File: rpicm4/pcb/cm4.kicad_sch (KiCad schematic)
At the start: 3 parts

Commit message: rpicm4
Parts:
- removed Module?: ComputeModule4-CM4, CM4IO:Raspberry-Pi-4-Compute-Module, symbol CM4IO:ComputeModule4-CM4
- added Module1: ComputeModule4-CM4, CM4IO:Raspberry-Pi-4-Compute-Module, symbol CM4IO:ComputeModule4-CM4
- J1, J2: renamed from J?; footprint (none) -> Connector_USB:USB_C_Receptacle_XKB_U262-16XN-4BVC11
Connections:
- net GND: now reaches J2.A1 (GND), J2.A12 (GND), J2.B1 (GND), J2.B12 (GND)
- net GND: now also J1.A1 (GND), J1.A12 (GND), J1.B1 (GND), J1.B12 (GND), J1.S1 (SHIELD), J2.S1 (SHIELD), Module1.1 (GND), Module1.107 (GND), Module1.108 (GND), Module1.113 (GND), Module1.114 (GND), Module1.119 (GND), Module1.120 (GND), Module1.125 (GND), Module1.126 (GND), Module1.13 (GND), Module1.131 (GND), Module1.132 (GND), Module1.137 (GND), Module1.138 (GND), Module1.14 (GND), Module1.144 (GND), Module1.150 (GND), Module1.155 (GND), Module1.156 (GND), Module1.161 (GND), Module1.162 (GND), Module1.167 (GND), Module1.168 (GND), Module1.173 (GND), Module1.179 (GND), Module1.180 (GND), Module1.185 (GND), Module1.186 (GND), Module1.191 (GND), Module1.192 (GND), Module1.197 (GND), Module1.198 (GND), Module1.2 (GND), Module1.22 (GND), Module1.23 (GND), Module1.32 (GND), Module1.33 (GND), Module1.42 (GND), Module1.43 (GND), Module1.52 (GND), Module1.53 (GND), Module1.59 (GND), Module1.60 (GND), Module1.65 (GND), Module1.66 (GND), Module1.7 (GND), Module1.71 (GND), Module1.74 (GND), Module1.8 (GND), Module1.98 (GND)
- net +5V: now reaches J2.A4 (VBUS), J2.A9 (VBUS), J2.B4 (VBUS), J2.B9 (VBUS)
- net +5V: now also J1.A4 (VBUS), J1.A9 (VBUS), J1.B4 (VBUS), J1.B9 (VBUS), Module1.77 (+5v_(Input)), Module1.79 (+5v_(Input)), Module1.81 (+5v_(Input)), Module1.83 (+5v_(Input)), Module1.85 (+5v_(Input)), Module1.87 (+5v_(Input))
- net USB_P: now reaches J2.A6 (D+)
- net USB_P: now also Module1.105 (USB2_P)
- net USB_N: now reaches J2.A7 (D-)
- net USB_N: now also Module1.103 (USB2_N)
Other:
- moved on the sheet: J2

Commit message: rpicm4 usb
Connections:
- net USB_N: now also J2.B7 (D-)
- net USB_P: now also J2.B6 (D+)
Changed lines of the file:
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@@
   (junction (at 73.7108 119.9388) (diameter 1.016) (color 0 0 0 0))
   (junction (at 73.7108 150.4188) (diameter 1.016) (color 0 0 0 0))
-  (junction (at 139.6492 127.5588) (diameter 1.016) (color 0 0 0 0))
-  (junction (at 139.6492 130.0988) (diameter 1.016) (color 0 0 0 0))
-  (junction (at 139.6492 132.6388) (diameter 1.016) (color 0 0 0 0))
-  (junction (at 139.6492 135.1788) (diameter 1.016) (color 0 0 0 0))
-  (junction (at 139.6492 137.7188) (diameter 1.016) (color 0 0 0 0))
+  (junction (at 142.24 127.5588) (diameter 1.016) (color 0 0 0 0))
+  (junction (at 142.24 130.0988) (diameter 1.016) (color 0 0 0 0))
+  (junction (at 142.24 132.6388) (diameter 1.016) (color 0 0 0 0))
+  (junction (at 142.24 135.1788) (diameter 1.016) (color 0 0 0 0))
+  (junction (at 142.24 137.7188) (diameter 1.016) (color 0 0 0 0))
   (junction (at 142.3416 36.1188) (diameter 1.016) (color 0 0 0 0))
   (junction (at 142.3416 43.7388) (diameter 1.016) (color 0 0 0 0))
@@
     (stroke (width 0) (type solid) (color 0 0 0 0))
   )
-  (wire (pts (xy 138.3792 125.0188) (xy 139.6492 125.0188))
-    (stroke (width 0) (type solid) (color 0 0 0 0))
-  )
-  (wire (pts (xy 138.3792 127.5588) (xy 139.6492 127.5588))
-    (stroke (width 0) (type solid) (color 0 0 0 0))
-  )
-  (wire (pts (xy 138.3792 130.0988) (xy 139.6492 130.0988))
-    (stroke (width 0) (type solid) (color 0 0 0 0))
-  )
-  (wire (pts (xy 138.3792 132.6388) (xy 139.6492 132.6388))
-    (stroke (width 0) (type solid) (color 0 0 0 0))
-  )
-  (wire (pts (xy 138.3792 135.1788) (xy 139.6492 135.1788))
-    (stroke (width 0) (type solid) (color 0 0 0 0))
-  )
-  (wire (pts (xy 138.3792 137.7188) (xy 139.6492 137.7188))
-    (stroke (width 0) (type solid) (color 0 0 0 0))
-  )
-  (wire (pts (xy 139.6492 125.0188) (xy 139.6492 127.5588))
-    (stroke (width 0) (type solid) (color 0 0 0 0))
-  )
-  (wire (pts (xy 139.6492 127.5588) (xy 139.6492 130.0988))
-    (stroke (width 0) (type solid) (color 0 0 0 0))
-  )
-  (wire (pts (xy 139.6492 130.0988) (xy 139.6492 132.6388))
-    (stroke (width 0) (type solid) (color 0 0 0 0))
-  )
-  (wire (pts (xy 139.6492 132.6388) (xy 139.6492 135.1788))
-    (stroke (width 0) (type solid) (color 0 0 0 0))
-  )
-  (wire (pts (xy 139.6492 135.1788) (xy 139.6492 137.7188))
-    (stroke (width 0) (type solid) (color 0 0 0 0))
-  )
-  (wire (pts (xy 139.6492 137.7188) (xy 142.24 137.7188))
+  (wire (pts (xy 138.3792 125.0188) (xy 142.24 125.0188))
+    (stroke (width 0) (type solid) (color 0 0 0 0))
+  )
+  (wire (pts (xy 138.3792 127.5588) (xy 142.24 127.5588))
+    (stroke (width 0) (type solid) (color 0 0 0 0))
+  )
+  (wire (pts (xy 138.3792 130.0988) (xy 142.24 130.0988))
+    (stroke (width 0) (type solid) (color 0 0 0 0))
+  )
+  (wire (pts (xy 138.3792 132.6388) (xy 142.24 132.6388))
+    (stroke (width 0) (type solid) (color 0 0 0 0))
+  )
+  (wire (pts (xy 138.3792 135.1788) (xy 142.24 135.1788))
+    (stroke (width 0) (type solid) (color 0 0 0 0))
+  )
+  (wire (pts (xy 138.3792 137.7188) (xy 142.24 137.7188))
+    (stroke (width 0) (type solid) (color 0 0 0 0))
+  )
+  (wire (pts (xy 142.24 125.0188) (xy 142.24 127.5588))
+    (stroke (width 0) (type solid) (color 0 0 0 0))
+  )
+  (wire (pts (xy 142.24 127.5588) (xy 142.24 130.0988))
+    (stroke (width 0) (type solid) (color 0 0 0 0))
+  )
+  (wire (pts (xy 142.24 130.0988) (xy 142.24 132.6388))
+    (stroke (width 0) (type solid) (color 0 0 0 0))
+  )
+  (wire (pts (xy 142.24 132.6388) (xy 142.24 135.1788))
+    (stroke (width 0) (type solid) (color 0 0 0 0))
+  )
+  (wire (pts (xy 142.24 135.1788) (xy 142.24 137.7188))
     (stroke (width 0) (type solid) (color 0 0 0 0))
   )
@@
     (stroke (width 0) (type solid) (color 0 0 0 0))
   )
+  (wire (pts (xy 147.6756 43.7388) (xy 147.6756 51.3588))
+    (stroke (width 0) (type solid) (color 0 0 0 0))
+  )
   (wire (pts (xy 147.6756 43.7388) (xy 148.844 43.7388))
     (stroke (width 0) (type solid) (color 0 0 0 0))
   )
-  (wire (pts (xy 147.6756 51.3588) (xy 147.6756 43.7388))
+  (wire (pts (xy 147.6756 51.3588) (xy 147.6756 58.9788))
     (stroke (width 0) (type solid) (color 0 0 0 0))
   )
@@
     (stroke (width 0) (type solid) (color 0 0 0 0))
   )
-  (wire (pts (xy 147.6756 58.9788) (xy 147.6756 51.3588))
-    (stroke (width 0) (type solid) (color 0 0 0 0))
-  )
   (wire (pts (xy 147.6756 58.9788) (xy 148.844 58.9788))
     (stroke (width 0) (type solid) (color 0 0 0 0))
@@
     (stroke (width 0) (type solid) (color 0 0 0 0))
   )
-  (wire (pts (xy 246.6848 91.9988) (xy 254.6096 91.9988))
+  (wire (pts (xy 246.6848 89.4588) (xy 251.1552 89.4588))
+    (stroke (width 0) (type solid) (color 0 0 0 0))
+  )
+  (wire (pts (xy 246.6848 91.9988) (xy 251.1552 91.9988))
+    (stroke (width 0) (type solid) (color 0 0 0 0))
+  )
+  (wire (pts (xy 246.6848 94.5388) (xy 251.1552 94.5388))
     (stroke (width 0) (type solid) (color 0 0 0 0))
   )
@@
     (effects (font (size 1.27 1.27)) (justify left bottom))
   )
-  (label "USB_P" (at 254.6096 91.9988 0)
-    (effects (font (size 1.27 1.27)) (justify left bottom))
-  )
+  (label "USB_N" (at 251.1552 89.4588 0)
+    (effects (font (size 1.27 1.27)) (justify left bottom))
+  )
+  (label "USB_P" (at 251.1552 91.9988 0)
+    (effects (font (size 1.27 1.27)) (justify left bottom))
+  )
+  (label "USB_P" (at 251.1552 94.5388 0)
+    (effects (font (size 1.27 1.27)) (justify left bottom))
+  )

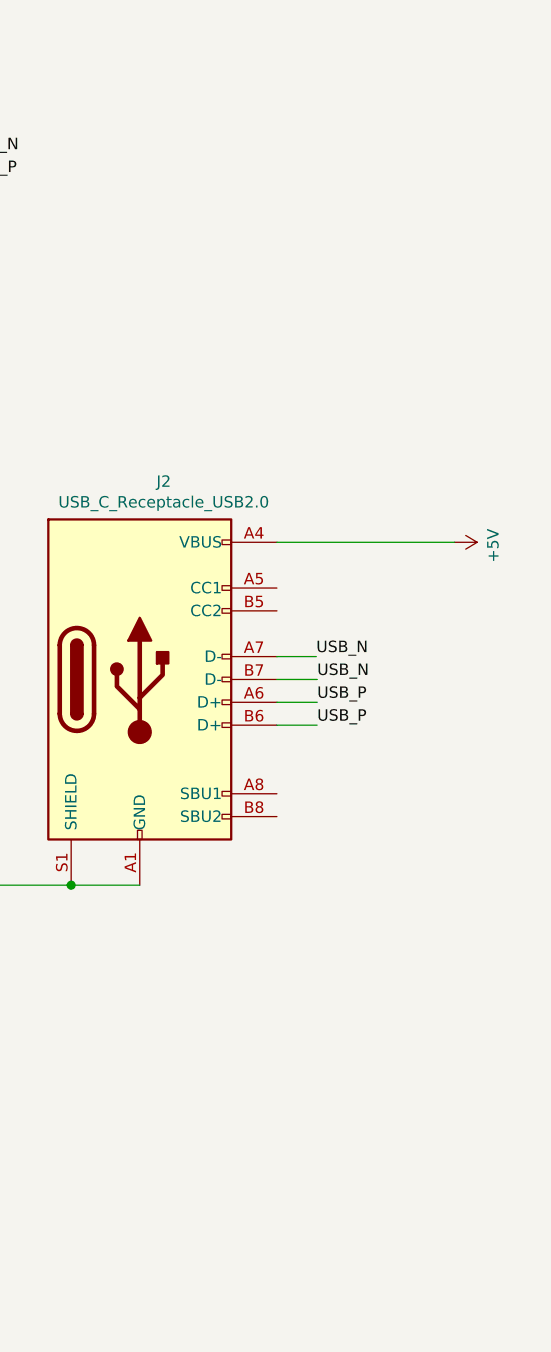
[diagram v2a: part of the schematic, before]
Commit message: rpicm4: typec ufp/dfp
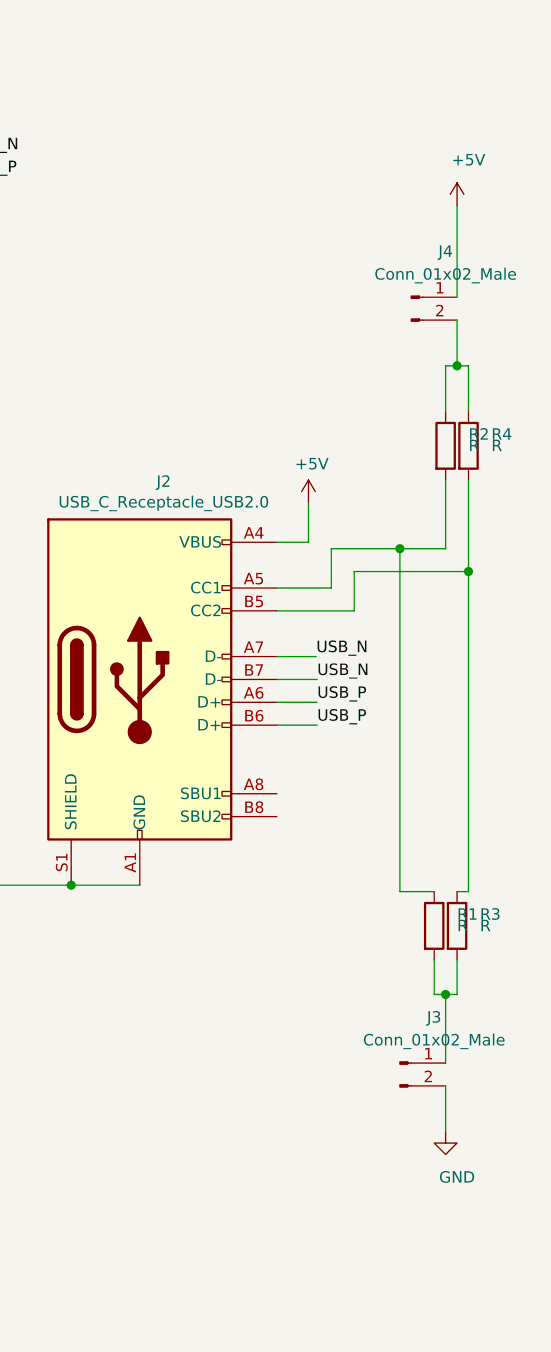
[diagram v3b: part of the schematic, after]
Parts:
- added J3, J4: Conn_01x02_Male, Connector_PinHeader_2.54mm:PinHeader_1x02_P2.54mm_Vertical, symbol Connector:Conn_01x02_Male
- added R1, R2, R3, R4: R, Resistor_THT:R_Axial_DIN0309_L9.0mm_D3.2mm_P12.70mm_Horizontal, symbol Device:R
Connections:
- net +5V: now also J4.1 (Pin_1)
- net GND: now also J3.2 (Pin_2)
- net at J2.A5 (CC1): now also R1.1, R2.2
- net at J2.B5 (CC2): now also R3.1, R4.2
- new net: J3.1 (Pin_1), R1.2, R3.2
- new net: J4.2 (Pin_2), R2.1, R4.1

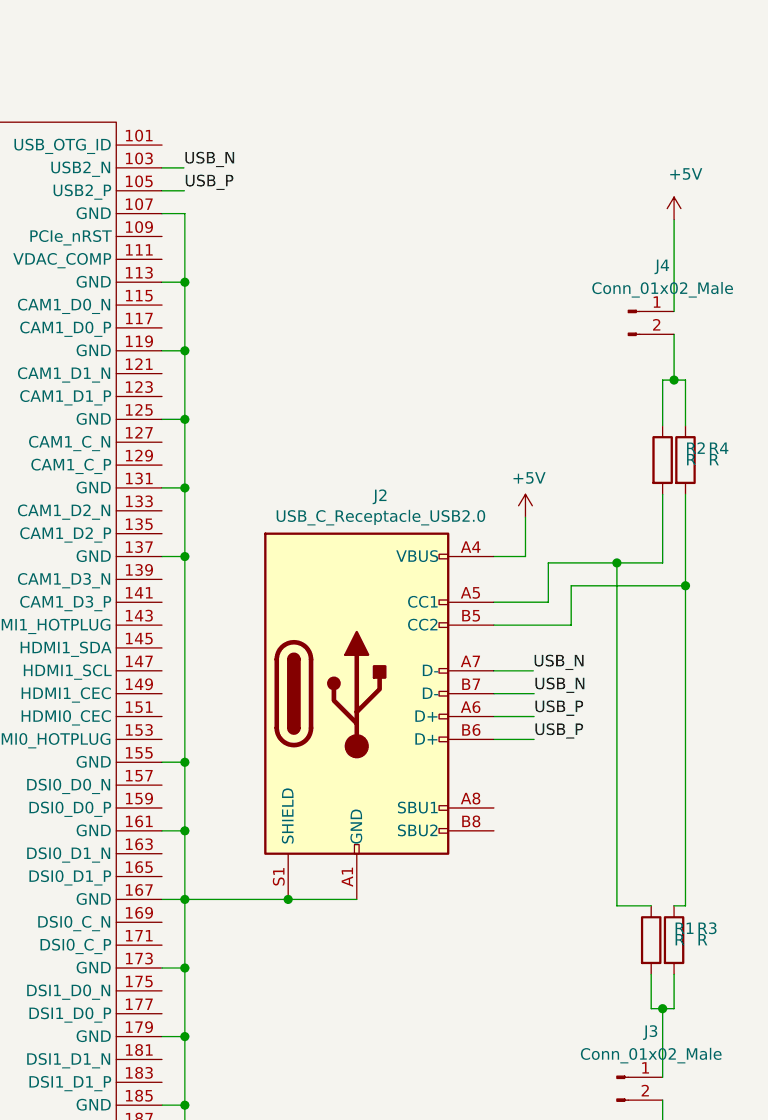
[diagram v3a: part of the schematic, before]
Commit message: rpicm4: dwc2 host/device
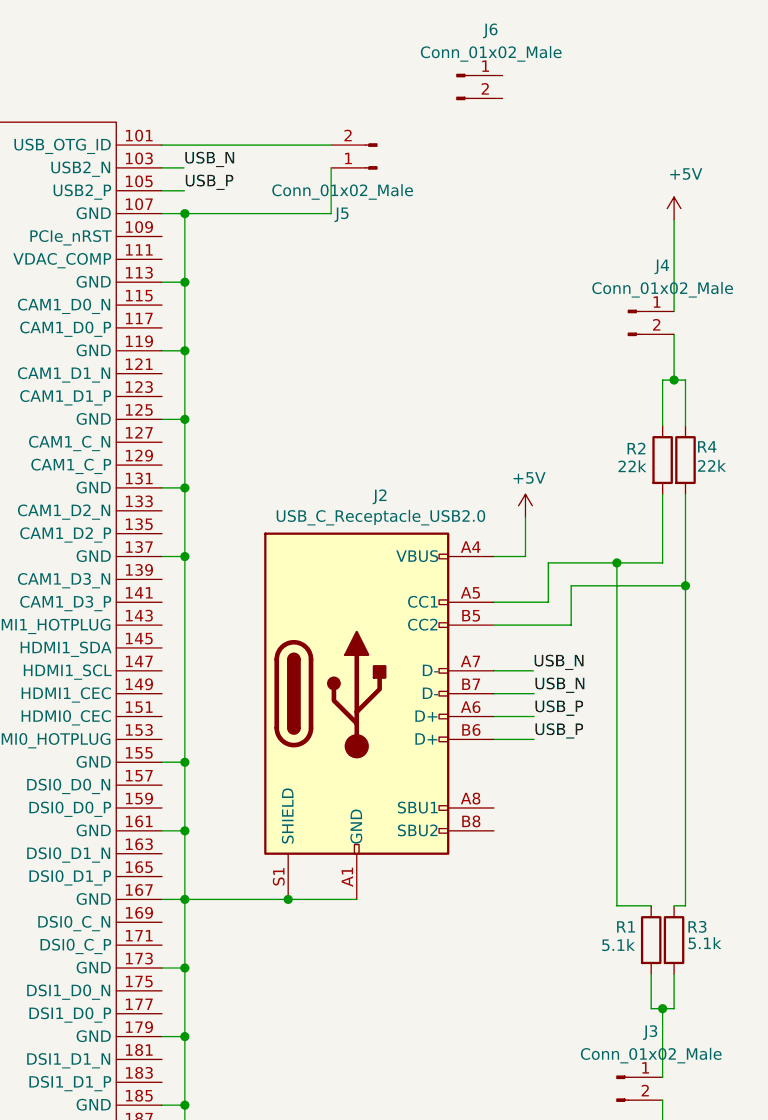
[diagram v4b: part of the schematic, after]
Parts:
- added J5, J6: Conn_01x02_Male, Connector_PinHeader_2.54mm:PinHeader_1x02_P2.54mm_Vertical, symbol Connector:Conn_01x02_Male
- R1, R3: value R -> 5.1k
- R2, R4: value R -> 22k
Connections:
- net GND: now also J5.1 (Pin_1)
- net at Module1.101 (USB_OTG_ID): now also J5.2 (Pin_2)
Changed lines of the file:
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@@
   (junction (at 147.6756 142.7988) (diameter 1.016) (color 0 0 0 0))
   (junction (at 147.6756 150.4188) (diameter 1.016) (color 0 0 0 0))
+  (junction (at 212.344 36.1188) (diameter 1.016) (color 0 0 0 0))
   (junction (at 212.344 43.7388) (diameter 1.016) (color 0 0 0 0))
   (junction (at 212.344 51.3588) (diameter 1.016) (color 0 0 0 0))
@@
     (stroke (width 0) (type solid) (color 0 0 0 0))
   )
+  (wire (pts (xy 209.804 28.4988) (xy 228.6 28.4988))
+    (stroke (width 0) (type solid) (color 0 0 0 0))
+  )
   (wire (pts (xy 209.804 31.0388) (xy 212.2424 31.0388))
     (stroke (width 0) (type solid) (color 0 0 0 0))
@@
   )
   (wire (pts (xy 223.8248 112.3188) (xy 231.4448 112.3188))
+    (stroke (width 0) (type solid) (color 0 0 0 0))
+  )
+  (wire (pts (xy 228.6 31.0388) (xy 228.6 36.1188))
+    (stroke (width 0) (type solid) (color 0 0 0 0))
+  )
+  (wire (pts (xy 228.6 36.1188) (xy 212.344 36.1188))
     (stroke (width 0) (type solid) (color 0 0 0 0))
   )
@@
   (symbol (lib_id "Device:R") (at 264.16 116.84 0) (unit 1)
     (in_bom yes) (on_board yes)
-    (property "Reference" "R1" (id 0) (at 266.7 115.57 0)
+    (property "Reference" "R1" (id 0) (at 260.1976 115.4176 0)
       (effects (font (size 1.27 1.27)) (justify left))
     )
-    (property "Value" "R" (id 1) (at 266.7 116.84 0)
+    (property "Value" "5.1k" (id 1) (at 258.572 117.4496 0)
       (effects (font (size 1.27 1.27)) (justify left))
     )
@@
   (symbol (lib_id "Device:R") (at 265.43 63.5 0) (unit 1)
     (in_bom yes) (on_board yes)
-    (property "Reference" "R2" (id 0) (at 267.97 62.23 0)
+    (property "Reference" "R2" (id 0) (at 261.366 62.2808 0)
       (effects (font (size 1.27 1.27)) (justify left))
     )
-    (property "Value" "R" (id 1) (at 267.97 63.5 0)
+    (property "Value" "22k" (id 1) (at 260.4006 64.2624 0)
       (effects (font (size 1.27 1.27)) (justify left))
     )
@@
   (symbol (lib_id "Device:R") (at 266.7 116.84 0) (unit 1)
     (in_bom yes) (on_board yes)
-    (property "Reference" "R3" (id 0) (at 269.24 115.57 0)
+    (property "Reference" "R3" (id 0) (at 268.1224 115.4176 0)
       (effects (font (size 1.27 1.27)) (justify left))
     )
-    (property "Value" "R" (id 1) (at 269.24 116.84 0)
+    (property "Value" "5.1k" (id 1) (at 268.1732 117.2464 0)
       (effects (font (size 1.27 1.27)) (justify left))
     )
@@
   (symbol (lib_id "Device:R") (at 267.97 63.5 0) (unit 1)
     (in_bom yes) (on_board yes)
-    (property "Reference" "R4" (id 0) (at 270.51 62.23 0)
+    (property "Reference" "R4" (id 0) (at 269.1892 62.0776 0)
       (effects (font (size 1.27 1.27)) (justify left))
     )
-    (property "Value" "R" (id 1) (at 270.51 63.5 0)
+    (property "Value" "22k" (id 1) (at 269.24 64.2112 0)
       (effects (font (size 1.27 1.27)) (justify left))
     )
@@
     )
     (property "Datasheet" "~" (id 3) (at 267.97 63.5 0)
+      (effects (font (size 1.27 1.27)) hide)
+    )
+  )
+  (symbol (lib_id "Connector:Conn_01x02_Male") (at 233.68 31.0388 180) (unit 1)
+    (in_bom yes) (on_board yes)
+    (property "Reference" "J5" (id 0) (at 229.87 36.1188 0))
+    (property "Value" "Conn_01x02_Male" (id 1) (at 229.87 33.5788 0))
+    (property "Footprint" "Connector_PinHeader_2.54mm:PinHeader_1x02_P2.54mm_Vertical" (id 2) (at 233.68 31.0388 0)
+      (effects (font (size 1.27 1.27)) hide)
+    )
+    (property "Datasheet" "~" (id 3) (at 233.68 31.0388 0)
+      (effects (font (size 1.27 1.27)) hide)
+    )
+  )
+  (symbol (lib_id "Connector:Conn_01x02_Male") (at 242.57 20.7772 0) (unit 1)
+    (in_bom yes) (on_board yes)
+    (property "Reference" "J6" (id 0) (at 246.38 15.6972 0))
+    (property "Value" "Conn_01x02_Male" (id 1) (at 246.38 18.2372 0))
+    (property "Footprint" "Connector_PinHeader_2.54mm:PinHeader_1x02_P2.54mm_Vertical" (id 2) (at 242.57 20.7772 0)
+      (effects (font (size 1.27 1.27)) hide)
+    )
+    (property "Datasheet" "~" (id 3) (at 242.57 20.7772 0)
       (effects (font (size 1.27 1.27)) hide)
     )
@@
       (reference "J4") (unit 1) (value "Conn_01x02_Male") (footprint "Connector_PinHeader_2.54mm:PinHeader_1x02_P2.54mm_Vertical")
     )
+    (path "/e20348d8-6a2f-4db8-bf42-c0c932ff98d2"
+      (reference "J5") (unit 1) (value "Conn_01x02_Male") (footprint "Connector_PinHeader_2.54mm:PinHeader_1x02_P2.54mm_Vertical")
+    )
+    (path "/05ba687f-5af6-4990-abfc-52c0bb0bba50"
+      (reference "J6") (unit 1) (value "Conn_01x02_Male") (footprint "Connector_PinHeader_2.54mm:PinHeader_1x02_P2.54mm_Vertical")
+    )
     (path "/485b1676-2be3-43f8-9a38-7962ea1aab1d"
       (reference "Module1") (unit 1) (value "ComputeModule4-CM4") (footprint "CM4IO:Raspberry-Pi-4-Compute-Module")
@@
     )
     (path "/7a966beb-4461-437e-b87c-ce3ac4e3f7a8"
-      (reference "R1") (unit 1) (value "R") (footprint "Resistor_THT:R_Axial_DIN0309_L9.0mm_D3.2mm_P12.70mm_Horizontal")
+      (reference "R1") (unit 1) (value "5.1k") (footprint "Resistor_THT:R_Axial_DIN0309_L9.0mm_D3.2mm_P12.70mm_Horizontal")
     )
     (path "/90638be6-e48d-471d-9808-51b737bfa37f"
-      (reference "R2") (unit 1) (value "R") (footprint "Resistor_THT:R_Axial_DIN0309_L9.0mm_D3.2mm_P12.70mm_Horizontal")
+      (reference "R2") (unit 1) (value "22k") (footprint "Resistor_THT:R_Axial_DIN0309_L9.0mm_D3.2mm_P12.70mm_Horizontal")
     )
     (path "/1b3e5f38-fb34-4109-8000-5da26ea3d377"
-      (reference "R3") (unit 1) (value "R") (footprint "Resistor_THT:R_Axial_DIN0309_L9.0mm_D3.2mm_P12.70mm_Horizontal")
+      (reference "R3") (unit 1) (value "5.1k") (footprint "Resistor_THT:R_Axial_DIN0309_L9.0mm_D3.2mm_P12.70mm_Horizontal")
     )
     (path "/721fe07a-3775-46f4-86f2-e2e56cd6ed9b"
-      (reference "R4") (unit 1) (value "R") (footprint "Resistor_THT:R_Axial_DIN0309_L9.0mm_D3.2mm_P12.70mm_Horizontal")
-    )
-  )
+      (reference "R4") (unit 1) (value "22k") (footprint "Resistor_THT:R_Axial_DIN0309_L9.0mm_D3.2mm_P12.70mm_Horizontal")
+    )
+  )

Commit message: rpicm4: usb mode
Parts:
- R1, R2, R3, R4: footprint Resistor_THT:R_Axial_DIN0309_L9.0mm_D3.2mm_P12.70mm_Horizontal -> Resistor_THT:R_Axial_DIN0207_L6.3mm_D2.5mm_P10.16mm_Horizontal
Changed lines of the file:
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@@
       (effects (font (size 1.27 1.27)) (justify left))
     )
-    (property "Footprint" "Resistor_THT:R_Axial_DIN0309_L9.0mm_D3.2mm_P12.70mm_Horizontal" (id 2) (at 262.382 116.84 90)
+    (property "Footprint" "Resistor_THT:R_Axial_DIN0207_L6.3mm_D2.5mm_P10.16mm_Horizontal" (id 2) (at 262.382 116.84 90)
       (effects (font (size 1.27 1.27)) hide)
     )
@@
       (effects (font (size 1.27 1.27)) (justify left))
     )
-    (property "Footprint" "Resistor_THT:R_Axial_DIN0309_L9.0mm_D3.2mm_P12.70mm_Horizontal" (id 2) (at 263.652 63.5 90)
+    (property "Footprint" "Resistor_THT:R_Axial_DIN0207_L6.3mm_D2.5mm_P10.16mm_Horizontal" (id 2) (at 263.652 63.5 90)
       (effects (font (size 1.27 1.27)) hide)
     )
@@
       (effects (font (size 1.27 1.27)) (justify left))
     )
-    (property "Footprint" "Resistor_THT:R_Axial_DIN0309_L9.0mm_D3.2mm_P12.70mm_Horizontal" (id 2) (at 264.922 116.84 90)
+    (property "Footprint" "Resistor_THT:R_Axial_DIN0207_L6.3mm_D2.5mm_P10.16mm_Horizontal" (id 2) (at 264.922 116.84 90)
       (effects (font (size 1.27 1.27)) hide)
     )
@@
       (effects (font (size 1.27 1.27)) (justify left))
     )
-    (property "Footprint" "Resistor_THT:R_Axial_DIN0309_L9.0mm_D3.2mm_P12.70mm_Horizontal" (id 2) (at 266.192 63.5 90)
+    (property "Footprint" "Resistor_THT:R_Axial_DIN0207_L6.3mm_D2.5mm_P10.16mm_Horizontal" (id 2) (at 266.192 63.5 90)
       (effects (font (size 1.27 1.27)) hide)
     )
@@
     )
     (path "/7a966beb-4461-437e-b87c-ce3ac4e3f7a8"
-      (reference "R1") (unit 1) (value "5.1k") (footprint "Resistor_THT:R_Axial_DIN0309_L9.0mm_D3.2mm_P12.70mm_Horizontal")
+      (reference "R1") (unit 1) (value "5.1k") (footprint "Resistor_THT:R_Axial_DIN0207_L6.3mm_D2.5mm_P10.16mm_Horizontal")
     )
     (path "/90638be6-e48d-471d-9808-51b737bfa37f"
-      (reference "R2") (unit 1) (value "22k") (footprint "Resistor_THT:R_Axial_DIN0309_L9.0mm_D3.2mm_P12.70mm_Horizontal")
+      (reference "R2") (unit 1) (value "22k") (footprint "Resistor_THT:R_Axial_DIN0207_L6.3mm_D2.5mm_P10.16mm_Horizontal")
     )
     (path "/1b3e5f38-fb34-4109-8000-5da26ea3d377"
-      (reference "R3") (unit 1) (value "5.1k") (footprint "Resistor_THT:R_Axial_DIN0309_L9.0mm_D3.2mm_P12.70mm_Horizontal")
+      (reference "R3") (unit 1) (value "5.1k") (footprint "Resistor_THT:R_Axial_DIN0207_L6.3mm_D2.5mm_P10.16mm_Horizontal")
     )
     (path "/721fe07a-3775-46f4-86f2-e2e56cd6ed9b"
-      (reference "R4") (unit 1) (value "22k") (footprint "Resistor_THT:R_Axial_DIN0309_L9.0mm_D3.2mm_P12.70mm_Horizontal")
-    )
-  )
+      (reference "R4") (unit 1) (value "22k") (footprint "Resistor_THT:R_Axial_DIN0207_L6.3mm_D2.5mm_P10.16mm_Horizontal")
+    )
+  )
